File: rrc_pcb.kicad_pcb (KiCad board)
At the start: 2 copper layers, 139 x 50.8 mm, 13 parts, among them J1 Voltage Regulator Input, J2 Conn_01x03_Male, U1 ADXL357Z, U2 Teensy3.6-teensy, U3 BN220-GPS, U4 MS5611, U5 logo

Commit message: fixed pcb trace issues
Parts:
- added REF**: MountingHole_2.1mm, MountingHole:MountingHole_2.1mm, F.Cu at (134.6, 116.8)
- added REF**: MountingHole_2.1mm, MountingHole:MountingHole_2.1mm, F.Cu at (78.7, 76.2)
- added REF**: MountingHole_2.1mm, MountingHole:MountingHole_2.1mm, F.Cu at (190.5, 63.5)
- added REF**: MountingHole_2.1mm, MountingHole:MountingHole_2.1mm, F.Cu at (127.0, 66.0)
- added REF**: MountingHole_2.1mm, MountingHole:MountingHole_2.1mm, F.Cu at (190.5, 119.4)
- moved J1 68.9 mm to (71.1, 68.6)
- moved BZ1 33.4 mm to (129.5, 85.1)
- moved RF11 22.1 mm to (155.3, 107.0), turned to 0 degrees
- moved U5 18.7 mm to (170.2, 83.8)
- moved J2 8.49 mm to (129.5, 99.1)
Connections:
- RF11 pad 10: Net-(RF11-Pad10) -> unconnected-(RF11-Pad10)
- RF11 pad 11: Net-(RF11-Pad11) -> unconnected-(RF11-Pad11)
- RF11 pad 12: Net-(RF11-Pad12) -> unconnected-(RF11-Pad12)
- RF11 pad 13: Net-(RF11-Pad13) -> unconnected-(RF11-Pad13)
- RF11 pad 14: Net-(RF11-Pad14) -> unconnected-(RF11-Pad14)
- RF11 pad 15: Net-(RF11-Pad15) -> unconnected-(RF11-Pad15)
- RF11 pad 16: Net-(RF11-Pad16) -> unconnected-(RF11-Pad16)
- RF11 pad 2: Net-(RF11-Pad2) -> unconnected-(RF11-Pad2)
- RF11 pad 3: Net-(RF11-Pad3) -> unconnected-(RF11-Pad3)
- RF11 pad 8: Net-(RF11-Pad8) -> unconnected-(RF11-Pad8)
- U1 pad 10: Net-(U1-Pad10) -> unconnected-(U1-Pad10)
- U1 pad 2: Net-(U1-Pad2) -> unconnected-(U1-Pad2)
- U1 pad 4: Net-(U1-Pad4) -> unconnected-(U1-Pad4)
- U1 pad 6: Net-(U1-Pad6) -> unconnected-(U1-Pad6)
- U1 pad 7: Net-(U1-Pad7) -> unconnected-(U1-Pad7)
- U1 pad 9: Net-(U1-Pad9) -> unconnected-(U1-Pad9)
- U2 pad 10: Net-(U2-Pad10) -> unconnected-(U2-Pad10)
- U2 pad 13: Net-(U2-Pad13) -> unconnected-(U2-Pad13)
- U2 pad 14: Net-(U2-Pad14) -> unconnected-(U2-Pad14)
- U2 pad 16: Net-(U2-Pad16) -> unconnected-(U2-Pad16)
- U2 pad 17: Net-(U2-Pad17) -> unconnected-(U2-Pad17)
- U2 pad 18: Net-(U2-Pad18) -> unconnected-(U2-Pad18)
- U2 pad 19: Net-(U2-Pad19) -> unconnected-(U2-Pad19)
- U2 pad 20: Net-(U2-Pad20) -> unconnected-(U2-Pad20)
- U2 pad 21: Net-(U2-Pad21) -> unconnected-(U2-Pad21)
- U2 pad 22: Net-(U2-Pad22) -> unconnected-(U2-Pad22)
- U2 pad 25: Net-(U2-Pad25) -> unconnected-(U2-Pad25)
- U2 pad 26: Net-(U2-Pad26) -> unconnected-(U2-Pad26)
- U2 pad 27: Net-(U2-Pad27) -> unconnected-(U2-Pad27)
- U2 pad 28: Net-(U2-Pad28) -> unconnected-(U2-Pad28)
- U2 pad 29: Net-(U2-Pad29) -> unconnected-(U2-Pad29)
- U2 pad 30: Net-(U2-Pad30) -> unconnected-(U2-Pad30)
- U2 pad 31: Net-(U2-Pad31) -> unconnected-(U2-Pad31)
- U2 pad 32: Net-(U2-Pad32) -> unconnected-(U2-Pad32)
- U2 pad 33: Net-(U2-Pad33) -> unconnected-(U2-Pad33)
- U2 pad 34: Net-(U2-Pad34) -> unconnected-(U2-Pad34)
- U2 pad 35: Net-(U2-Pad35) -> unconnected-(U2-Pad35)
- U2 pad 36: Net-(U2-Pad36) -> unconnected-(U2-Pad36)
- U2 pad 37: Net-(U2-Pad37) -> unconnected-(U2-Pad37)
- U2 pad 38: Net-(U2-Pad38) -> unconnected-(U2-Pad38)
- U2 pad 4: Net-(U2-Pad4) -> unconnected-(U2-Pad4)
- U2 pad 40: Net-(U2-Pad40) -> unconnected-(U2-Pad40)
- U2 pad 41: Net-(U2-Pad41) -> unconnected-(U2-Pad41)
- U2 pad 42: Net-(U2-Pad42) -> unconnected-(U2-Pad42)
- U2 pad 43: Net-(U2-Pad43) -> unconnected-(U2-Pad43)
- U2 pad 44: Net-(U2-Pad44) -> unconnected-(U2-Pad44)
- U2 pad 47: Net-(U2-Pad47) -> unconnected-(U2-Pad47)
- U2 pad 48: Net-(U2-Pad48) -> unconnected-(U2-Pad48)
- U2 pad 49: Net-(U2-Pad49) -> unconnected-(U2-Pad49)
- U2 pad 50: Net-(U2-Pad50) -> unconnected-(U2-Pad50)
- U2 pad 51: Net-(U2-Pad51) -> unconnected-(U2-Pad51)
- U2 pad 52: Net-(U2-Pad52) -> unconnected-(U2-Pad52)
- U2 pad 54: Net-(U2-Pad54) -> unconnected-(U2-Pad54)
- U2 pad 55: Net-(U2-Pad55) -> unconnected-(U2-Pad55)
- U2 pad 56: Net-(U2-Pad56) -> unconnected-(U2-Pad56)
- U2 pad 57: Net-(U2-Pad57) -> unconnected-(U2-Pad57)
- U2 pad 7: Net-(U2-Pad7) -> unconnected-(U2-Pad7)
- U2 pad 8: Net-(U2-Pad8) -> unconnected-(U2-Pad8)
- U2 pad 9: Net-(U2-Pad9) -> unconnected-(U2-Pad9)
- U4 pad 5: Net-(U4-Pad5) -> unconnected-(U4-Pad5)
- U4 pad 6: Net-(U4-Pad6) -> unconnected-(U4-Pad6)
- U4 pad 7: Net-(U4-Pad7) -> unconnected-(U4-Pad7)
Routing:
- net T_GND: track 0.00 -> 191.4 mm, vias 0 -> 2
- net T_VCC: track 25.1 -> 120.9 mm
- net GND: track 80.0 -> 128.2 mm
- net VCC: track 122.8 -> 149.0 mm
- net Net-(BZ1-Pad1): track 42.6 -> 17.8 mm
- net Net-(RF11-Pad7): track 79.8 -> 101.5 mm, vias 0 -> 1
- net Net-(RF11-Pad9): track 96.5 -> 112.6 mm
- net Net-(J2-Pad2): track 23.2 -> 14.1 mm
- net Net-(RF11-Pad4): track 2.54 -> 0.00 mm
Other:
- board size 139 x 50.8 mm -> 139 x 68.6 mm
- net class Default removed

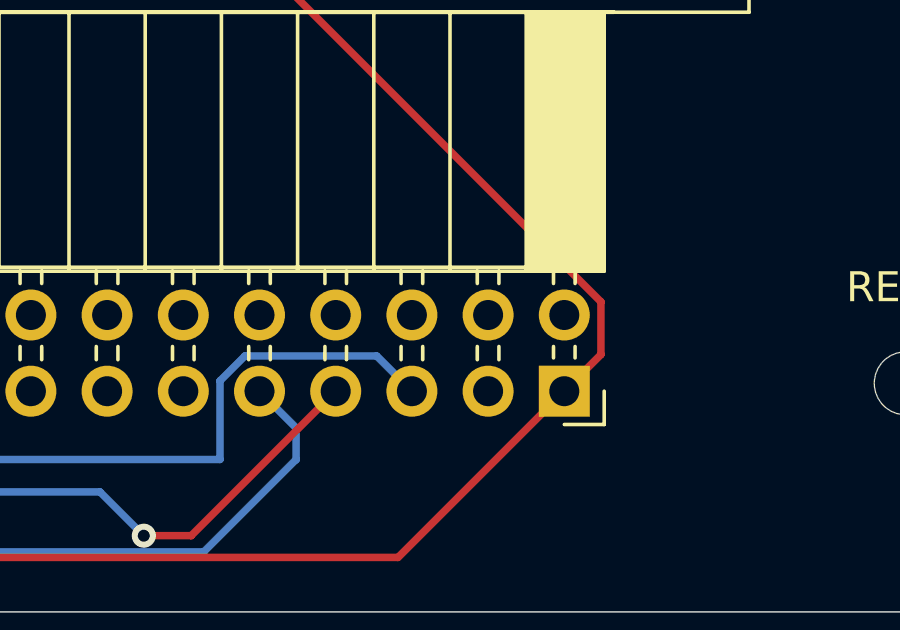
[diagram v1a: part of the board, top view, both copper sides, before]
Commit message: fixed pcb traces and moved stuff around
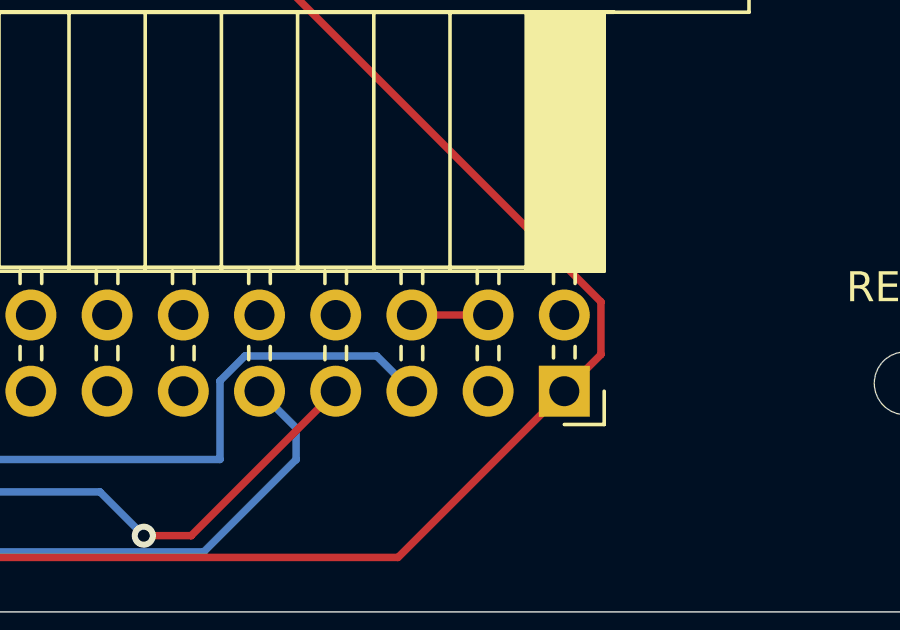
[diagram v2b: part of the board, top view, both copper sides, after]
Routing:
- net Net-(RF11-Pad4): track 0.00 -> 2.54 mm
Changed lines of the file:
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@@
   (segment (start 163.64 123) (end 165.1 124.46) (width 0.25) (layer "B.Cu") (net 11))
   (segment (start 89.916 109.728) (end 89.916 99.806) (width 0.25) (layer "B.Cu") (net 11))
+  (segment (start 174.03726 117.10344) (end 176.57726 117.10344) (width 0.25) (layer "F.Cu") (net 12))
   (segment (start 87 117.157002) (end 87.027001 117.130001) (width 0.25) (layer "B.Cu") (net 14))
   (segment (start 87 119.231002) (end 87 117.157002) (width 0.25) (layer "B.Cu") (net 14))

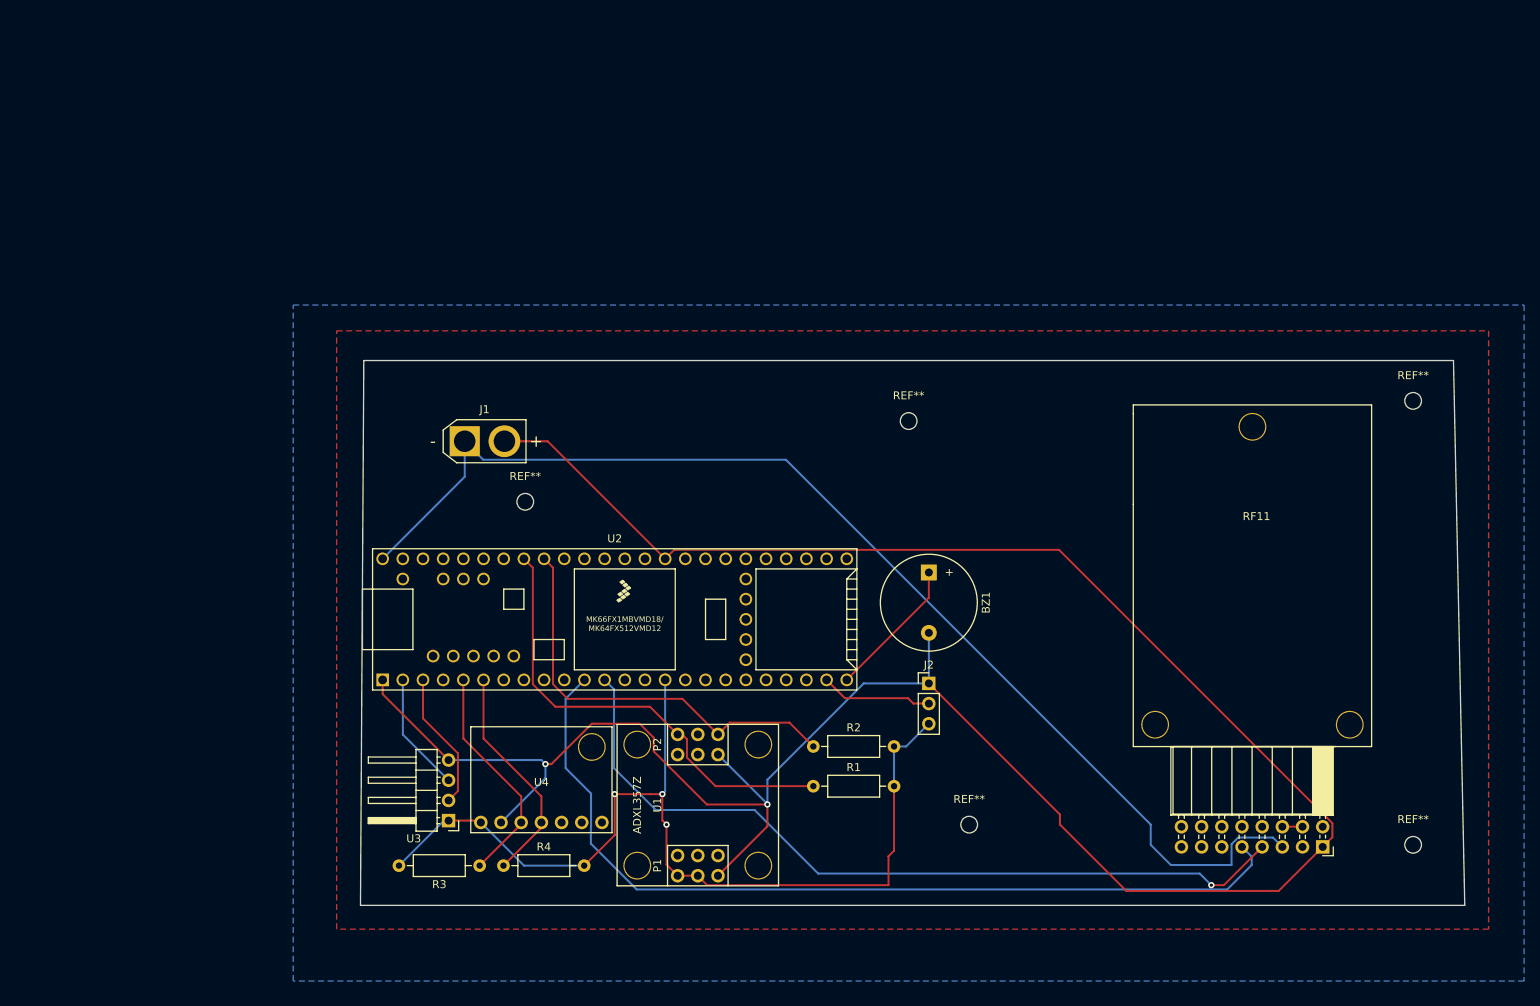
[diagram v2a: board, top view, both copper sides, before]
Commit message: edited gps mount
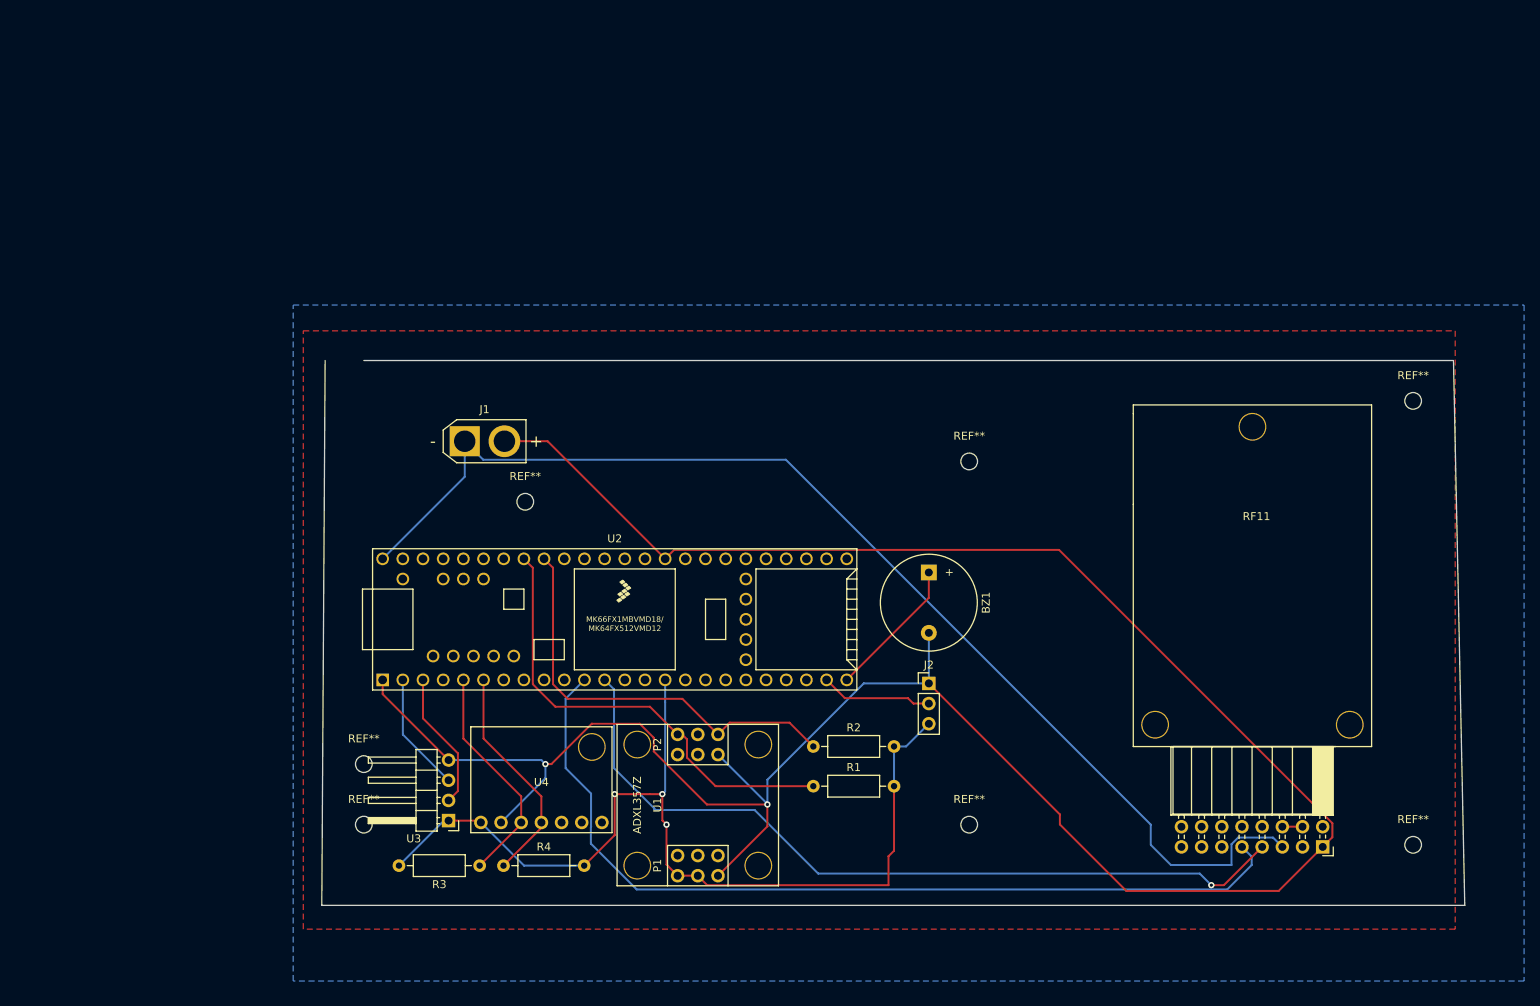
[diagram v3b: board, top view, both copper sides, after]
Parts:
- added REF**: MountingHole_2.1mm, MountingHole:MountingHole_2.1mm, F.Cu at (58.4, 116.8)
- added REF**: MountingHole_2.1mm, MountingHole:MountingHole_2.1mm, F.Cu at (58.4, 109.2)
- moved REF** 9.16 mm to (134.6, 71.1)
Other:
- board size 139 x 68.6 mm -> 143.9 x 68.6 mm
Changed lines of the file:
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@@
+  )
+  (footprint "MountingHole:MountingHole_2.1mm" (layer "F.Cu")
+    (at 58.42 116.84)
+    (descr "Mounting Hole 2.1mm, no annular")
+    (tags "mounting hole 2.1mm no annular")
+    (attr exclude_from_pos_files exclude_from_bom)
+    (fp_text reference "REF**" (at 0 -3.2) (layer "F.SilkS")
+      (effects (font (size 1 1) (thickness 0.15)))
+    )
+    (fp_text value "MountingHole_2.1mm" (at 0 3.2) (layer "F.Fab")
+      (effects (font (size 1 1) (thickness 0.15)))
+    )
+    (fp_text user "${REFERENCE}" (at 0 0) (layer "F.Fab")
+      (effects (font (size 1 1) (thickness 0.15)))
+    )
+    (fp_circle (center 0 0) (end 2.1 0) (layer "Cmts.User") (width 0.15) (fill none))
+    (fp_circle (center 0 0) (end 2.35 0) (layer "F.CrtYd") (width 0.05) (fill none))
+    (pad "" np_thru_hole circle (at 0 0) (size 2.1 2.1) (drill 2.1) (layers *.Cu *.Mask))
   )
   (footprint "MountingHole:MountingHole_2.1mm" (layer "F.Cu")
     (at 78.74 76.2)
+    (descr "Mounting Hole 2.1mm, no annular")
+    (tags "mounting hole 2.1mm no annular")
+    (attr exclude_from_pos_files exclude_from_bom)
+    (fp_text reference "REF**" (at 0 -3.2) (layer "F.SilkS")
+      (effects (font (size 1 1) (thickness 0.15)))
+    )
+    (fp_text value "MountingHole_2.1mm" (at 0 3.2) (layer "F.Fab")
+      (effects (font (size 1 1) (thickness 0.15)))
+    )
+    (fp_text user "${REFERENCE}" (at 0 0) (layer "F.Fab")
+      (effects (font (size 1 1) (thickness 0.15)))
+    )
+    (fp_circle (center 0 0) (end 2.1 0) (layer "Cmts.User") (width 0.15) (fill none))
+    (fp_circle (center 0 0) (end 2.35 0) (layer "F.CrtYd") (width 0.05) (fill none))
+    (pad "" np_thru_hole circle (at 0 0) (size 2.1 2.1) (drill 2.1) (layers *.Cu *.Mask))
+  )
+  (footprint "MountingHole:MountingHole_2.1mm" (layer "F.Cu")
+    (at 58.42 109.22)
     (descr "Mounting Hole 2.1mm, no annular")
     (tags "mounting hole 2.1mm no annular")
@@
   )
   (footprint "MountingHole:MountingHole_2.1mm" (layer "F.Cu")
-    (at 127 66.04)
+    (at 134.62 71.12)
     (descr "Mounting Hole 2.1mm, no annular")
     (tags "mounting hole 2.1mm no annular")
@@
       ) (layer "Eco2.User") (width 0.01) (fill solid))
   )
-  (gr_line (start 58 127) (end 58.42 58.42) (layer "Edge.Cuts") (width 0.05))
-  (gr_line (start 197 127) (end 58 127) (layer "Edge.Cuts") (width 0.05))
+  (gr_line (start 53.13 127) (end 53.55 58.42) (layer "Edge.Cuts") (width 0.05))
+  (gr_line (start 197 127) (end 53.13 127) (layer "Edge.Cuts") (width 0.05))
   (gr_line (start 195.58 58.42) (end 197 127) (layer "Edge.Cuts") (width 0.05))
   (gr_line (start 195.58 58.42) (end 58.42 58.42) (layer "Edge.Cuts") (width 0.05))
@@
     (polygon
       (pts
-        (xy 200 130)
-        (xy 55 130)
-        (xy 55 54.68)
-        (xy 200 54.68)
+        (xy 195.8 130)
+        (xy 50.8 130)
+        (xy 50.8 54.68)
+        (xy 195.8 54.68)
       )
     )
